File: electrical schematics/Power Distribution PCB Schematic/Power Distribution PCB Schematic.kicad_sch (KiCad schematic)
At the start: 62 parts, among them J1 XT60_Port, J10 Encoder_Header, J11 Encoder_Header, J12 Encoder_Header, J13 6VA_Converter_Input_Screw, J14 6VB_Converter_Input_Screw, J15 6VA_Converter_Output_Screw, J16 6VA_Servo_Power_Screw, J17 6VB_Servo_Power_Screw, J18 6VB_Converter_Output_Screw, J19 ServoPWM_Header, J2 On/Off_Switch_Screw_Terminal, J3 IMU_Header, J4 Raspberry_Pi_4, J5 BDC_Motor_Screw_Terminal, J6 BDC_Motor_Screw_Terminal, J7 BDC_Motor_Screw_Terminal, J8 BDC_Motor_Screw_Terminal, J9 Encoder_Header, U1 BDC_DRIVER_1, U2 BDC_DRIVER_2

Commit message: PCB Layout and Schematic Finalization
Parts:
- removed 470ohm2: R_US, symbol Device:R_US
- removed 5V_Converter1: ~, symbol Rover_Project:5V_Voltage_Regulator_-_D36V28F5
- removed C9: 68nF, symbol Device:C
- removed GPS_Module1: ~, symbol Rover_Project:GPS_Module
- removed J13: 6VA_Converter_Input_Screw, symbol Connector:Screw_Terminal_01x02
- removed J14: 6VB_Converter_Input_Screw, symbol Connector:Screw_Terminal_01x02
- removed J15: 6VA_Converter_Output_Screw, symbol Connector:Screw_Terminal_01x02
- removed J16: 6VA_Servo_Power_Screw, symbol Connector:Screw_Terminal_01x02
- removed J17: 6VB_Servo_Power_Screw, symbol Connector:Screw_Terminal_01x02
- removed J18: 6VB_Converter_Output_Screw, symbol Connector:Screw_Terminal_01x02
- removed J19: ServoPWM_Header, symbol Connector_Generic:Conn_01x05
- removed J2: On/Off_Switch_Screw_Terminal, symbol Connector:Screw_Terminal_01x02
- removed J3: IMU_Header, symbol Connector_Generic:Conn_01x05
- removed U1: BDC_DRIVER_1, Package_SO:SSOP-24_5.3x8.2mm_P0.65mm, symbol Driver_Motor:TB6612FNG
- removed U2: BDC_DRIVER_2, Package_SO:SSOP-24_5.3x8.2mm_P0.65mm, symbol Driver_Motor:TB6612FNG
- added 180ohm2: R_US, Resistor_THT:R_Axial_DIN0207_L6.3mm_D2.5mm_P7.62mm_Horizontal, symbol Device:R_US
- added C6: 10uF, Capacitor_THT:CP_Radial_D4.0mm_P2.00mm, symbol Device:C
- added Driver_Board1, Driver_Board2: ~, Rover_Project.:Motor Driver Board, symbol Rover_Project:Dual_Channel_Motor_Driver
- added J16: 6V_to_Motors_Screw, Rover_Project.:01x04_Screw_Terminal, symbol Connector:Screw_Terminal_01x04
- added J2: 12V_6V_Input_Screw, Rover_Project.:01x03_Screw_Terminal, symbol Connector:Screw_Terminal_01x03
- added J20: 5V_Regulator_Header, Connector_PinHeader_2.54mm:PinHeader_1x05_P2.54mm_Vertical, symbol Connector_Generic:Conn_01x05
- added J21: GPS_Module_Header, Connector_PinHeader_2.54mm:PinHeader_1x05_P2.54mm_Vertical, symbol Connector_Generic:Conn_01x05
- added J3: 6V_Output_Screw, Rover_Project.:01x04_Screw_Terminal, symbol Connector:Screw_Terminal_01x04
- added J4: IMU_Module_Header, Connector_PinHeader_2.54mm:PinHeader_1x08_P2.54mm_Vertical, symbol Connector_Generic:Conn_01x08
- added J5: Magnetometer_Module_Header, Connector_PinHeader_2.54mm:PinHeader_1x04_P2.54mm_Vertical, symbol Connector_Generic:Conn_01x04
- added J7: Servo_PWM_Header, Connector_PinHeader_2.54mm:PinHeader_1x08_P2.54mm_Vertical, symbol Connector_Generic:Conn_01x08
- 10k1, 33k1: footprint (none) -> Resistor_THT:R_Axial_DIN0207_L6.3mm_D2.5mm_P7.62mm_Horizontal
- 150ohm1: renamed from R1; footprint (none) -> Resistor_THT:R_Axial_DIN0207_L6.3mm_D2.5mm_P7.62mm_Horizontal
- 180ohm1: renamed from 470ohm1; footprint (none) -> Resistor_THT:R_Axial_DIN0207_L6.3mm_D2.5mm_P7.62mm_Horizontal
- 330uF1, C5: footprint (none) -> Capacitor_THT:CP_Radial_D4.0mm_P2.00mm
- 510ohm1: renamed from 1k1; footprint (none) -> Resistor_THT:R_Axial_DIN0207_L6.3mm_D2.5mm_P7.62mm_Horizontal
- C1: renamed from C6; value 68nF -> 0.1uF; footprint (none) -> Capacitor_THT:CP_Radial_D4.0mm_P2.00mm
- C10: footprint (none) -> Capacitor_THT:CP_Radial_D6.3mm_P2.50mm
- C2: renamed from C7; footprint (none) -> Capacitor_THT:CP_Radial_D6.3mm_P2.50mm
- C3: renamed from C1; footprint (none) -> Capacitor_THT:CP_Radial_D6.3mm_P2.50mm
- C4: renamed from C2; value 68nF -> 0.1uF; footprint (none) -> Capacitor_THT:CP_Radial_D4.0mm_P2.00mm
- C7: renamed from C4; value 68nF -> 0.1uF; footprint (none) -> Capacitor_THT:CP_Radial_D4.0mm_P2.00mm
- C8: value 10uF -> 0.1uF; footprint (none) -> Capacitor_THT:CP_Radial_D4.0mm_P2.00mm
- C9: renamed from C3; footprint (none) -> Capacitor_THT:CP_Radial_D6.3mm_P2.50mm
- D1, D2, D3, D4: footprint (none) -> LED_THT:LED_D3.0mm
- F1: footprint (none) -> Rover_Project.:Fuse_TH_5A
- J1: footprint (none) -> Connector_AMASS:AMASS_XT60-F_1x02_P7.20mm_Vertical
- J10: renamed from J7; footprint (none) -> Rover_Project.:01x03_Screw_Terminal
- J11: renamed from J8; footprint (none) -> Rover_Project.:01x03_Screw_Terminal
- J12: renamed from J9; footprint (none) -> Connector_PinHeader_2.54mm:PinHeader_1x03_P2.54mm_Vertical
- J13: renamed from J10; footprint (none) -> Connector_PinHeader_2.54mm:PinHeader_1x03_P2.54mm_Vertical
- J14: renamed from J11; footprint (none) -> Connector_PinHeader_2.54mm:PinHeader_1x03_P2.54mm_Vertical
- J15: renamed from J12; footprint (none) -> Connector_PinHeader_2.54mm:PinHeader_1x03_P2.54mm_Vertical
- J6: renamed from J4; footprint (none) -> Rover_Project.:SULLINS_PPTC202LFBN-RC
- J8: renamed from J5; footprint (none) -> Rover_Project.:01x03_Screw_Terminal
- J9: renamed from J6; footprint (none) -> Rover_Project.:01x03_Screw_Terminal
- R1: renamed from R2; footprint (none) -> Resistor_THT:R_Axial_DIN0207_L6.3mm_D2.5mm_P7.62mm_Horizontal
- R10: renamed from R11; footprint (none) -> Resistor_THT:R_Axial_DIN0207_L6.3mm_D2.5mm_P7.62mm_Horizontal
- R11: renamed from R12; footprint (none) -> Resistor_THT:R_Axial_DIN0207_L6.3mm_D2.5mm_P7.62mm_Horizontal
- R12: renamed from R13; footprint (none) -> Resistor_THT:R_Axial_DIN0207_L6.3mm_D2.5mm_P7.62mm_Horizontal
- R13: renamed from R14; footprint (none) -> Resistor_THT:R_Axial_DIN0207_L6.3mm_D2.5mm_P7.62mm_Horizontal
- R14: renamed from R15; footprint (none) -> Resistor_THT:R_Axial_DIN0207_L6.3mm_D2.5mm_P7.62mm_Horizontal
- R15: renamed from R16; footprint (none) -> Resistor_THT:R_Axial_DIN0207_L6.3mm_D2.5mm_P7.62mm_Horizontal
- R16: renamed from R17; footprint (none) -> Resistor_THT:R_Axial_DIN0207_L6.3mm_D2.5mm_P7.62mm_Horizontal
- R2: renamed from R3; footprint (none) -> Resistor_THT:R_Axial_DIN0207_L6.3mm_D2.5mm_P7.62mm_Horizontal
- R3: renamed from R4; footprint (none) -> Resistor_THT:R_Axial_DIN0207_L6.3mm_D2.5mm_P7.62mm_Horizontal
- R4: renamed from R5; footprint (none) -> Resistor_THT:R_Axial_DIN0207_L6.3mm_D2.5mm_P7.62mm_Horizontal
- R5: renamed from R6; footprint (none) -> Resistor_THT:R_Axial_DIN0207_L6.3mm_D2.5mm_P7.62mm_Horizontal
- R6: renamed from R7; footprint (none) -> Resistor_THT:R_Axial_DIN0207_L6.3mm_D2.5mm_P7.62mm_Horizontal
- R7: renamed from R8; footprint (none) -> Resistor_THT:R_Axial_DIN0207_L6.3mm_D2.5mm_P7.62mm_Horizontal
- R8: renamed from R9; footprint (none) -> Resistor_THT:R_Axial_DIN0207_L6.3mm_D2.5mm_P7.62mm_Horizontal
- R9: renamed from R10; footprint (none) -> Resistor_THT:R_Axial_DIN0207_L6.3mm_D2.5mm_P7.62mm_Horizontal
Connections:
- net 12V_Bus: now also Driver_Board1.7 (VMOT), Driver_Board2.7 (VMOT), J2.1 (M+), J2.2 (M-), J20.2 (Vin)
- net 5V_Bus: now also Driver_Board1.2 (VCC), Driver_Board2.2 (VCC), J21.1 (VCC), J4.1 (Pin_1), J5.1 (VCC)
- net GND: now also C6.2, Driver_Board1.1 (GND), Driver_Board1.16 (GND), Driver_Board1.8 (GND), Driver_Board2.1 (GND), Driver_Board2.16 (GND), Driver_Board2.8 (GND), J16.1 (Pin_1), J16.4 (Pin_4), J2.3 (GND), J20.3 (GND), J20.4 (GND), J21.2 (GND), J3.1 (Pin_1), J3.4 (Pin_4), J4.2 (Pin_2), J4.7 (Pin_7), J5.2 (GND)
- net at R12.1, R6.1: now also J6.16 (GPIO23/SDIO_CMD); no longer J6.13 (GPIO27/SDIO_DAT3)
- net at J8.1 (M+): now also Driver_Board1.3 (AO1)
- net at J9.1 (M+): now also Driver_Board1.6 (BO1)
- net at A1.6 (GPIO4): now also Driver_Board1.13 (BIN1)
- net at A1.1 (GPIO0): now also Driver_Board1.9 (PWMA)
- net at A1.2 (GPIO1): now also Driver_Board1.10 (AIN2)
- net at A1.9 (GPIO6): now also Driver_Board1.15 (PWMB)
- net at A1.5 (GPIO3): now also Driver_Board1.12 (STBY), Driver_Board2.12 (STBY)
- net at A1.4 (GPIO2): now also Driver_Board1.11 (AIN1)
- net at A1.7 (GPIO5): now also Driver_Board1.14 (BIN2)
- net at J8.2 (M-): now also Driver_Board1.4 (AO2)
- net at J9.2 (M-): now also Driver_Board1.5 (BO2)
- net 6V_A: now reaches C10.1, C8.1
- net 6V_A: now also 180ohm2.1, C6.1, J16.2 (Pin_2), J3.2 (Pin_2)
- net at A1.10 (GPIO7): now also Driver_Board2.9 (PWMA)
- net at A1.11 (GPIO8): now also Driver_Board2.10 (AIN2)
- net at A1.12 (GPIO9): now also Driver_Board2.11 (AIN1)
- net at A1.14 (GPIO10): now also Driver_Board2.13 (BIN1)
- net at A1.15 (GPIO11): now also Driver_Board2.14 (BIN2)
- net at A1.16 (GPIO12): now also Driver_Board2.15 (PWMB)
- net at A1.17 (GPIO13): now also J7.3 (Pin_3)
- net at A1.19 (GPIO14): now also J7.2 (Pin_2)
- net at A1.20 (GPIO15): now also J7.1 (Pin_1)
- net at A1.21 (GPIO16): now also J7.8 (Pin_8)
- net at A1.22 (GPIO17): now also J7.7 (Pin_7)
- net at A1.24 (GPIO18): now also J7.6 (Pin_6)
- net at A1.25 (GPIO19): now also J7.5 (Pin_5)
- net at A1.26 (GPIO20): now also J7.4 (Pin_4)
- net at R1.1, R13.1: now also J6.37 (GPIO26/SDIO_DAT2); no longer J6.15 (GPIO22/SDIO_CLK)
- net at R14.1, R2.1: now also J6.31 (GPCLK2/GPIO06); no longer J6.16 (GPIO23/SDIO_CMD)
- net at R3.1, R9.1: now also J6.29 (GPCLK1/GPIO05); no longer J6.18 (GPIO24/SDIO_DAT0)
- net at J6.21 (MISO_SPI0/GPIO09): now also J21.5 (PPS)
- net at J6.24 (~{CE0}_SPI0/GPIO08): now also J21.4 (RXD)
- net at J6.26 (~{CE1}_SPI0/GPIO07): now also J21.3 (TXD)
- net at R16.1, R8.1: now also J6.13 (GPIO27/SDIO_DAT3); no longer J6.29 (GPCLK1/GPIO05)
- net at J6.3 (SDA_I2C1/GPIO02): now also J4.4 (Pin_4), J5.3 (SDA)
- net at R15.1, R7.1: now also J6.15 (GPIO22/SDIO_CLK); no longer J6.31 (GPCLK2/GPIO06)
- net at R11.1, R5.1: now also J6.18 (GPIO24/SDIO_DAT0); no longer J6.37 (GPIO26/SDIO_DAT2)
- net at J6.5 (SCL_I2C1/GPIO03): now also J4.3 (Pin_3), J5.4 (SCL)
- net at J6.7 (GPCLK0/GPIO04): now also J4.8 (Pin_8)
- net at D4.2 (A): now also 180ohm2.2
- net at F1.2: now also J20.5 (Vout)
- net at J10.1 (M+): now also Driver_Board2.3 (AO1)
- net at J11.1 (M+): now also Driver_Board2.6 (BO1)
- net at J10.2 (M-): now also Driver_Board2.4 (AO2)
- net at J11.2 (M-): now also Driver_Board2.5 (BO2)
- net 6V_B: now reaches 180ohm1.1, C5.1, C7.1, C9.1
- net 6V_B: now also J16.3 (Pin_3), J3.3 (Pin_3)
- no-connect marks 25 -> 22
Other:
- note added: "6V_A"
- note added: "6V_B"
- note added: "ADO"
- note added: "Battery->50A Fuse-> On/Off Switch->PCB"
- note added: "Both STBY pins are connected to the same Pico output pin"
- note added: "Converter ground signals"
- note added: "EN"
- note added: "Externally mounted to rover "head" Yes you will want a rover head. For camera module as well, add head turning servo?"
- note added: "Extra pwm connections for room for future motors (only need 5 currently) - 1 for camera head swivel - 2 for back wheel steering"
- note added: "IMPORTANT: CHECK ALL SENSOR OUTPUTS BEFORE CONNECTING TO THE PI. SHOULD NOT BE 5V"
- note added: "Motor ground signals"
- note added: "PPS"
- note added: "RXD"
- note added: "TXD"
- note added: "Vin"
- note added: "Vout"
- note added: "XCL"
- note added: "XDA"
- note removed: "Comes with internal pull-up resistors for I2C communication"
- note removed: "Double check that all signal lines output 3.3V highs NOT 5V = damage"
- note removed: "Had to add this short to represent the external switch as connected for the ERC to work."
- moved on the sheet: 150ohm1, 180ohm1, 330uF1, A1, C3, C4, C5, C7, C9, D2, D3, F1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

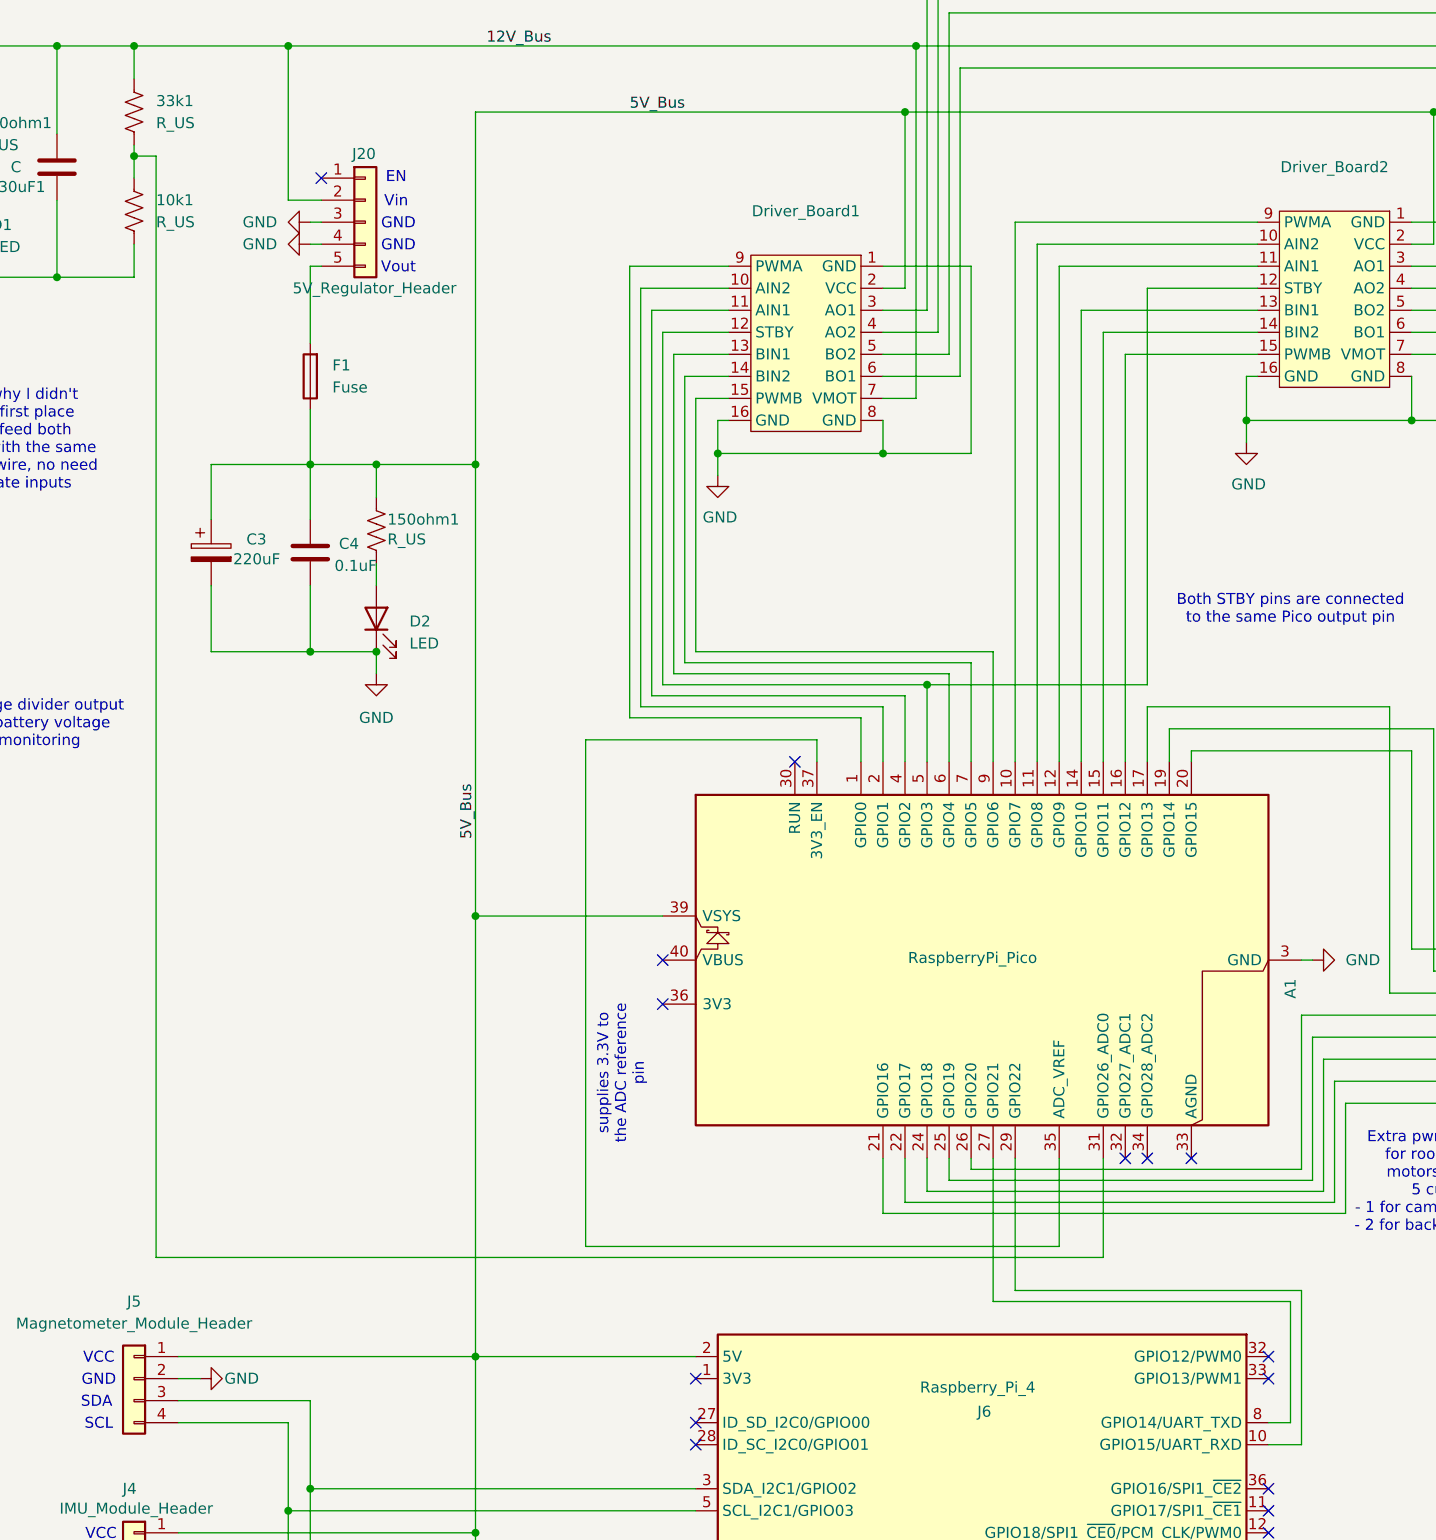
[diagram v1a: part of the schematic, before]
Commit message: Electrical System Modifications
Forgot about the ultrasonic sensor, added to PCB schematic + layout
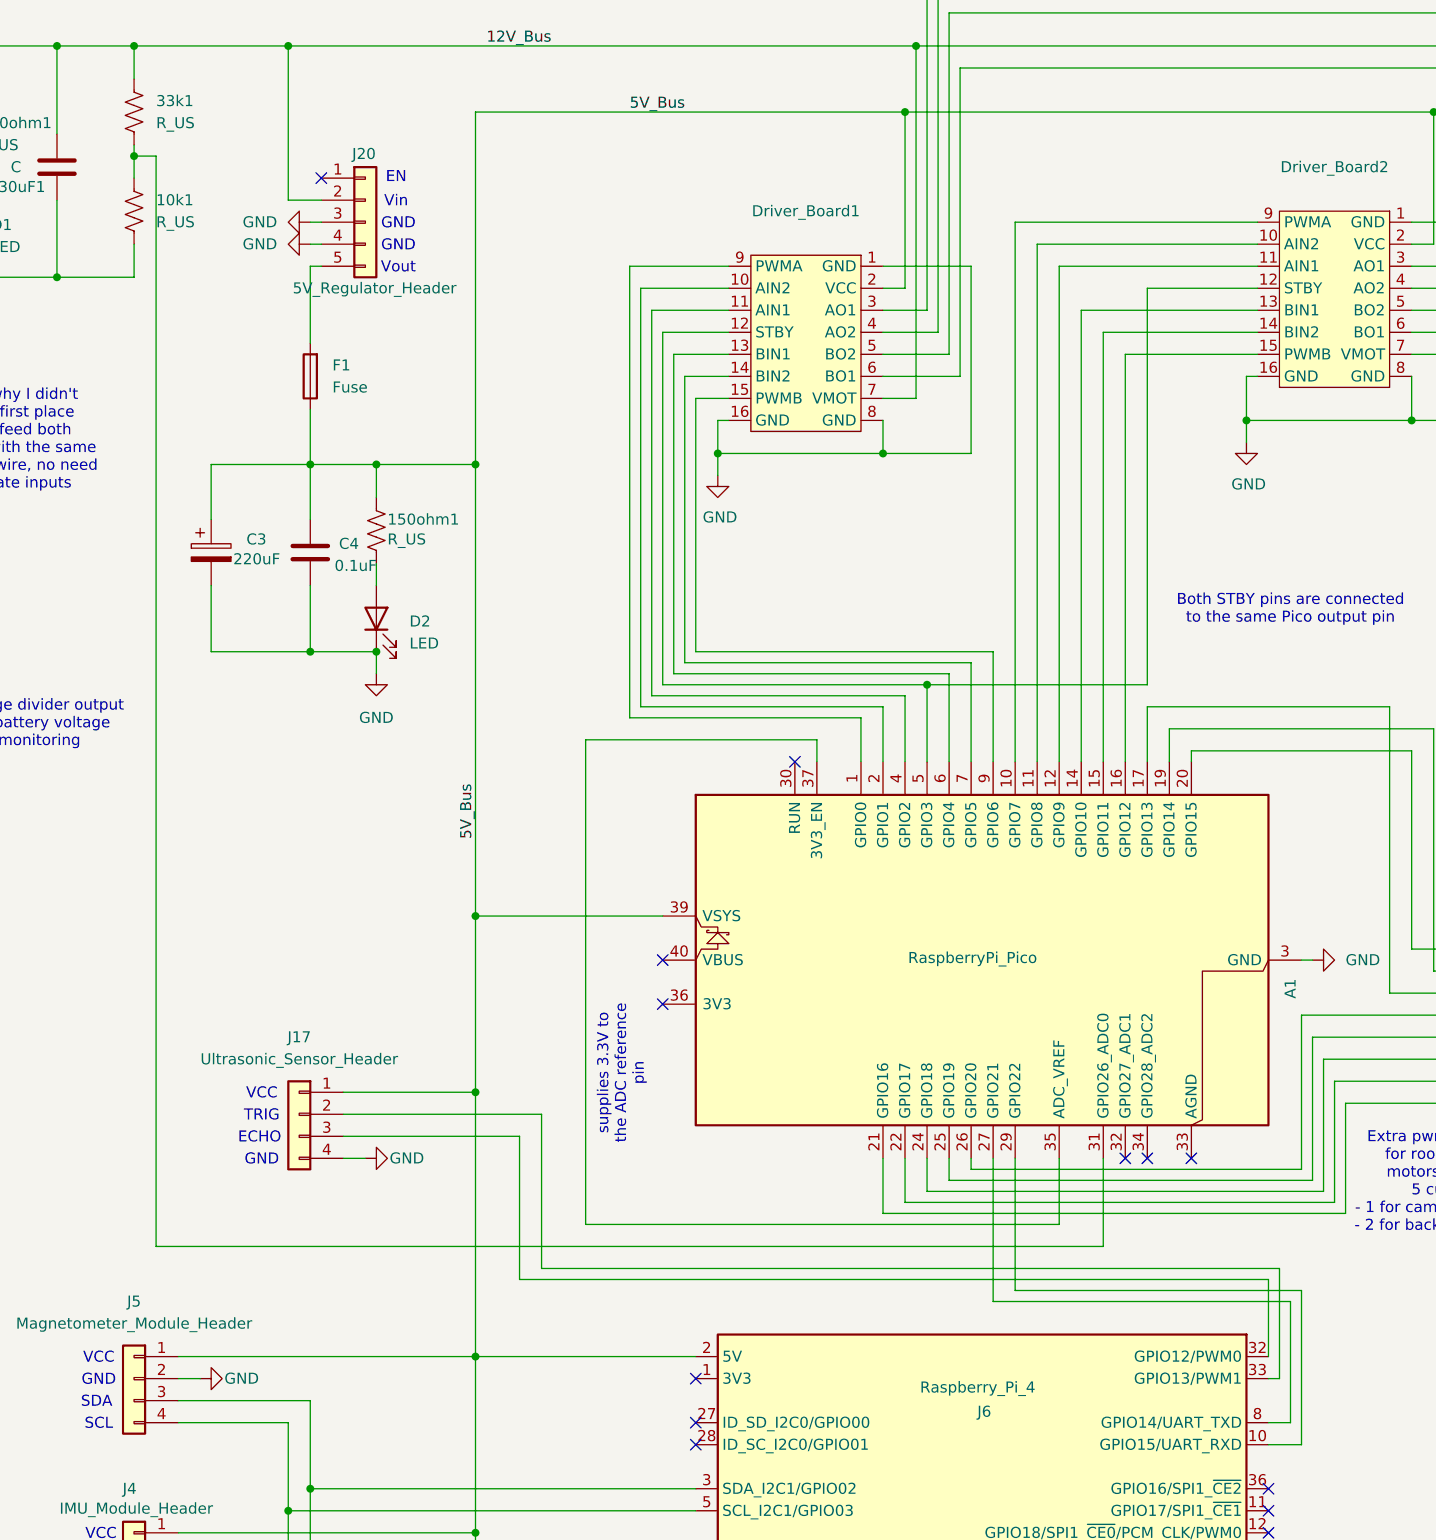
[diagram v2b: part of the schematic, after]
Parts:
- added J17: Ultrasonic_Sensor_Header, Connector_PinHeader_2.54mm:PinHeader_1x04_P2.54mm_Vertical, symbol Connector_Generic:Conn_01x04
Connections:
- net 5V_Bus: now also J17.1 (VCC)
- net GND: now also J17.4 (GND)
- net at J6.32 (GPIO12/PWM0): now also J17.3 (Echo)
- net at J6.33 (GPIO13/PWM1): now also J17.2 (Trig)
- no-connect marks 22 -> 20
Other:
- note added: "ECHO"
- note added: "TRIG"

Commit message: PCB Layout Adjustments + Drivetrain Design
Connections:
- net GND: now also D1.2 (K), D2.2 (K), D3.2 (K), D4.2 (K); no longer D1.1 (K), D2.1 (K), D3.1 (K), D4.1 (K)
- net at 510ohm1.2: now also D1.1 (A); no longer D1.2 (A)
- net at 150ohm1.2: now also D2.1 (A); no longer D2.2 (A)
- net at 180ohm2.2: now also D4.1 (A); no longer D4.2 (A)
- net at 180ohm1.2: now also D3.1 (A); no longer D3.2 (A)
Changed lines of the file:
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@@
 	)
 	(symbol
+		(lib_name "LED_1")
 		(lib_id "Device:LED")
 		(at 59.69 52.07 90)
@@
 	)
 	(symbol
+		(lib_name "LED_2")
 		(lib_id "Device:LED")
 		(at 398.78 71.12 180)
@@
 	)
 	(symbol
+		(lib_name "LED_3")
 		(lib_id "Device:LED")
 		(at 340.36 71.12 0)

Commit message: PCB Schematic v2
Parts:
- removed 180ohm1, 180ohm2: R_US, Resistor_THT:R_Axial_DIN0207_L6.3mm_D2.5mm_P7.62mm_Horizontal, symbol Device:R_US
- removed C10, C9: 220uF, Capacitor_THT:CP_Radial_D6.3mm_P2.50mm, symbol Device:C_Polarized
- removed C5, C6: 10uF, Capacitor_THT:CP_Radial_D4.0mm_P2.00mm, symbol Device:C
- removed C7, C8: 0.1uF, Capacitor_THT:CP_Radial_D4.0mm_P2.00mm, symbol Device:C
- removed D3, D4: LED, LED_THT:LED_D3.0mm, symbol Device:LED
- removed J16: 6V_to_Motors_Screw, Rover_Project.:01x04_Screw_Terminal, symbol Connector:Screw_Terminal_01x04
- removed J2: 12V_6V_Input_Screw, Rover_Project.:01x03_Screw_Terminal, symbol Connector:Screw_Terminal_01x03
- removed J3: 6V_Output_Screw, Rover_Project.:01x04_Screw_Terminal, symbol Connector:Screw_Terminal_01x04
- added To_6VA_Conv1: To_6VA_Converter, Rover_Project_2:12AWG Screw Terminal, symbol Connector:Screw_Terminal_01x02
- added To_6VB_Conv1: To_6VB_Convertor, Rover_Project_2:12AWG Screw Terminal, symbol Connector:Screw_Terminal_01x02
- 330uF1, C1, C4: footprint Capacitor_THT:CP_Radial_D4.0mm_P2.00mm -> Rover_Project_2:Ceramic Cap
- Driver_Board1, Driver_Board2: footprint Rover_Project.:Motor Driver Board -> Rover_Project_2:Motor Driver Board
- F1: footprint Rover_Project.:Fuse_TH_5A -> Rover_Project_2:Fuse_TH_5A
- J10: renamed from J9; footprint Rover_Project.:01x03_Screw_Terminal -> Rover_Project_2:01x03_Screw_Terminal
- J11: renamed from J10; footprint Rover_Project.:01x03_Screw_Terminal -> Rover_Project_2:01x03_Screw_Terminal
- J12: renamed from J11; footprint Rover_Project.:01x03_Screw_Terminal -> Rover_Project_2:01x03_Screw_Terminal
- J7: renamed from J6; footprint Rover_Project.:SULLINS_PPTC202LFBN-RC -> Rover_Project_2:SULLINS_PPTC202LFBN-RC
- J9: renamed from J8; footprint Rover_Project.:01x03_Screw_Terminal -> Rover_Project_2:01x03_Screw_Terminal
- renumbered J12 to J13, J13 to J14, J14 to J15, J15 to J16, J5 to J2, J4 to J3, J21 to J4, J17 to J5, J20 to J6, J7 to J8
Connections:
- net 12V_Bus: now also To_6VA_Conv1.2 (Pin_2), To_6VB_Conv1.2 (Pin_2)
- net GND: now also To_6VA_Conv1.1 (Pin_1), To_6VB_Conv1.1 (Pin_1)
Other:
- note removed: "6V_A"
- note removed: "6V_B"
- note removed: "Converter ground signals"
- note removed: "Motor ground signals"
